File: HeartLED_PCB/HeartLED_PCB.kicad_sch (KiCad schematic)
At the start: 33 parts, among them U1 ICM7555CBAZ, U2 CD4017BM, U3 HT7750A, U4 HX SS12F44G4

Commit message: Added LCSC and 3D models
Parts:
- BT1: LCSC (none) -> C5370859
- C1: LCSC (none) -> C1705
- C2: LCSC (none) -> C7190
- C3: footprint FOOTPRINTS:TAJA476K006RNJ -> FOOTPRINTS:TAJA226M010RNJ; LCSC (none) -> C7183
- L1: LCSC (none) -> C1034
- R1: LCSC (none) -> C15458
- R10, R11, R12, R3, R4, R5, R6, R7, R8, R9: LCSC (none) -> C25936
- R2: LCSC (none) -> C25531
- S1: LCSC (none) -> C727113
- U1: LCSC (none) -> C3304410
- U2: LCSC (none) -> C1523359
- U3: LCSC (none) -> C259884; LCSC Part C259884 -> (none)
- U4: LCSC (none) -> C5149844; LCSC Part C5149844 -> (none)
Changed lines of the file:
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@@
 			)
 		)
+		(property "LCSC" "C25936"
+			(at 96.52 78.74 90)
+			(effects
+				(font
+					(size 1.27 1.27)
+				)
+				(hide yes)
+			)
+		)
 		(pin "2"
 		)
@@
 			)
 		)
+		(property "LCSC" "C25936"
+			(at 96.52 86.36 90)
+			(effects
+				(font
+					(size 1.27 1.27)
+				)
+				(hide yes)
+			)
+		)
 		(pin "2"
 		)
@@
 			)
 		)
+		(property "LCSC" "C25936"
+			(at 96.52 91.44 90)
+			(effects
+				(font
+					(size 1.27 1.27)
+				)
+				(hide yes)
+			)
+		)
 		(pin "2"
 		)
@@
 			)
 		)
+		(property "LCSC" "C25936"
+			(at 96.52 88.9 90)
+			(effects
+				(font
+					(size 1.27 1.27)
+				)
+				(hide yes)
+			)
+		)
 		(pin "2"
 		)
@@
 			)
 		)
+		(property "LCSC" "C25936"
+			(at 96.52 71.12 90)
+			(effects
+				(font
+					(size 1.27 1.27)
+				)
+				(hide yes)
+			)
+		)
 		(pin "2"
 		)
@@
 			)
 		)
+		(property "LCSC" "C7190"
+			(at 40.64 172.72 0)
+			(effects
+				(font
+					(size 1.27 1.27)
+				)
+				(hide yes)
+			)
+		)
 		(pin "2"
 		)
@@
 			)
 		)
+		(property "LCSC" "C15458"
+			(at 20.32 26.67 90)
+			(effects
+				(font
+					(size 1.27 1.27)
+				)
+				(hide yes)
+			)
+		)
 		(pin "2"
 		)
@@
 			)
 		)
+		(property "LCSC" "C1705"
+			(at 20.32 31.75 90)
+			(effects
+				(font
+					(size 1.27 1.27)
+				)
+				(hide yes)
+			)
+		)
 		(pin "2"
 		)
@@
 			)
 		)
+		(property "LCSC" "C3304410"
+			(at 58.42 29.21 0)
+			(effects
+				(font
+					(size 1.27 1.27)
+				)
+				(hide yes)
+			)
+		)
 		(pin "7"
 		)
@@
 			)
 		)
+		(property "LCSC" "C25936"
+			(at 96.52 73.66 90)
+			(effects
+				(font
+					(size 1.27 1.27)
+				)
+				(hide yes)
+			)
+		)
 		(pin "2"
 		)
@@
 			)
 		)
-		(property "LCSC Part" "C259884"
-			(at 62.23 185.42 0)
+		(property "LCSC" "C259884"
+			(at 62.23 170.18 0)
 			(effects
 				(font
@@
 			)
 		)
+		(property "LCSC" "C5370859"
+			(at 62.23 125.73 0)
+			(effects
+				(font
+					(size 1.27 1.27)
+				)
+				(hide yes)
+			)
+		)
 		(pin "1"
 		)
@@
 			)
 		)
+		(property "LCSC" "C1523359"
+			(at 59.69 86.36 0)
+			(effects
+				(font
+					(size 1.27 1.27)
+				)
+				(hide yes)
+			)
+		)
 		(pin "2"
 		)
@@
 			)
 		)
-		(property "Footprint" "FOOTPRINTS:TAJA476K006RNJ"
+		(property "Footprint" "FOOTPRINTS:TAJA226M010RNJ"
 			(at 79.7052 176.53 0)
 			(effects
@@
 			)
 		)
+		(property "LCSC" "C7183"
+			(at 78.74 172.72 0)
+			(effects
+				(font
+					(size 1.27 1.27)
+				)
+				(hide yes)
+			)
+		)
 		(pin "1"
 		)
@@
 			)
 		)
-		(property "LCSC Part" "C5149844"
-			(at 62.23 125.73 0)
+		(property "LCSC" "C5149844"
+			(at 62.23 138.43 0)
 			(effects
 				(font
@@
 			)
 		)
+		(property "LCSC" "C25936"
+			(at 96.52 81.28 90)
+			(effects
+				(font
+					(size 1.27 1.27)
+				)
+				(hide yes)
+			)
+		)
 		(pin "2"
 		)
@@
 			)
 		)
+		(property "LCSC" "C25936"
+			(at 96.52 76.2 90)
+			(effects
+				(font
+					(size 1.27 1.27)
+				)
+				(hide yes)
+			)
+		)
 		(pin "2"
 		)
@@
 			)
 		)
+		(property "LCSC" "C25936"
+			(at 96.52 83.82 90)
+			(effects
+				(font
+					(size 1.27 1.27)
+				)
+				(hide yes)
+			)
+		)
 		(pin "2"
 		)
@@
 			)
 		)
+		(property "LCSC" "C25531"
+			(at 90.17 26.67 90)
+			(effects
+				(font
+					(size 1.27 1.27)
+				)
+				(hide yes)
+			)
+		)
 		(pin "2"
 		)
@@
 			)
 		)
+		(property "LCSC" "C727113"
+			(at 62.23 157.48 0)
+			(effects
+				(font
+					(size 1.27 1.27)
+				)
+				(hide yes)
+			)
+		)
 		(pin "1"
 		)
@@
 			)
 		)
+		(property "LCSC" "C25936"
+			(at 96.52 68.58 90)
+			(effects
+				(font
+					(size 1.27 1.27)
+				)
+				(hide yes)
+			)
+		)
 		(pin "2"
 		)
@@
 			(effects
 				(font
+					(size 1.27 1.27)
+				)
+				(hide yes)
+			)
+		)
+		(property "LCSC" "C1034"
+			(at 45.72 157.48 90)
+			(effects
+				(font

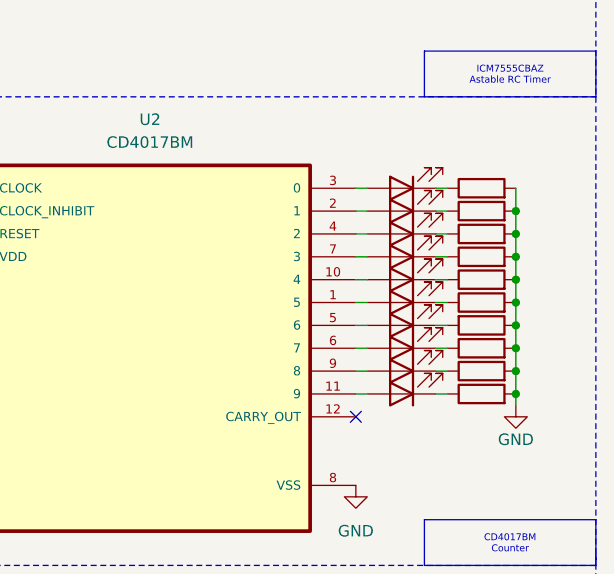
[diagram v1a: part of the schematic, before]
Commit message: Changed inductor
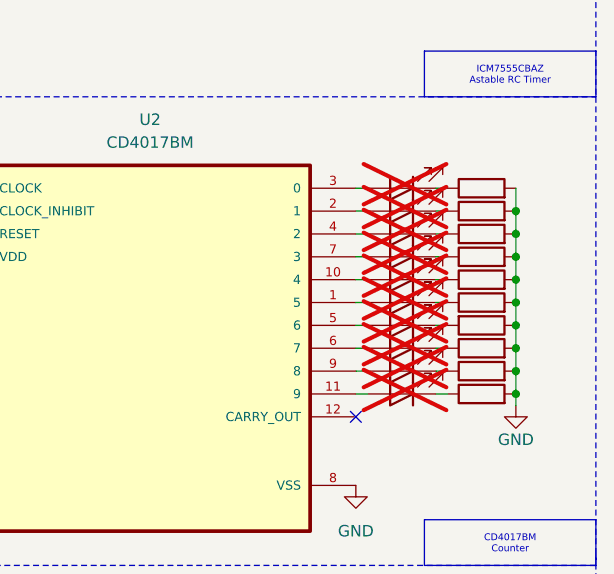
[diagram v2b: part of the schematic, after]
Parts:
- D1, D10, D2, D3, D4, D5, D6, D7, D8, D9: now not fitted
- L1: footprint FOOTPRINTS:SDFL1608Q4R7KTF -> FOOTPRINTS:SMNR5040-470MT
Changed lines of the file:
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@@
 		(in_bom yes)
 		(on_board yes)
-		(dnp no)
+		(dnp yes)
 		(fields_autoplaced yes)
 		(property "Reference" "D1"
@@
 		(in_bom yes)
 		(on_board yes)
-		(dnp no)
+		(dnp yes)
 		(fields_autoplaced yes)
 		(property "Reference" "D10"
@@
 		(in_bom yes)
 		(on_board yes)
-		(dnp no)
+		(dnp yes)
 		(fields_autoplaced yes)
 		(property "Reference" "D3"
@@
 		(in_bom yes)
 		(on_board yes)
-		(dnp no)
+		(dnp yes)
 		(fields_autoplaced yes)
 		(property "Reference" "D8"
@@
 		(in_bom yes)
 		(on_board yes)
-		(dnp no)
+		(dnp yes)
 		(fields_autoplaced yes)
 		(property "Reference" "D9"
@@
 		(in_bom yes)
 		(on_board yes)
-		(dnp no)
+		(dnp yes)
 		(fields_autoplaced yes)
 		(property "Reference" "D6"
@@
 		(in_bom yes)
 		(on_board yes)
-		(dnp no)
+		(dnp yes)
 		(fields_autoplaced yes)
 		(property "Reference" "D7"
@@
 		(in_bom yes)
 		(on_board yes)
-		(dnp no)
+		(dnp yes)
 		(fields_autoplaced yes)
 		(property "Reference" "D4"
@@
 		(in_bom yes)
 		(on_board yes)
-		(dnp no)
+		(dnp yes)
 		(fields_autoplaced yes)
 		(property "Reference" "D5"
@@
 		(in_bom yes)
 		(on_board yes)
-		(dnp no)
+		(dnp yes)
 		(fields_autoplaced yes)
 		(property "Reference" "D2"
@@
 			)
 		)
-		(property "Footprint" "FOOTPRINTS:SDFL1608Q4R7KTF"
+		(property "Footprint" "FOOTPRINTS:SMNR5040-470MT"
 			(at 45.72 157.48 0)
 			(effects

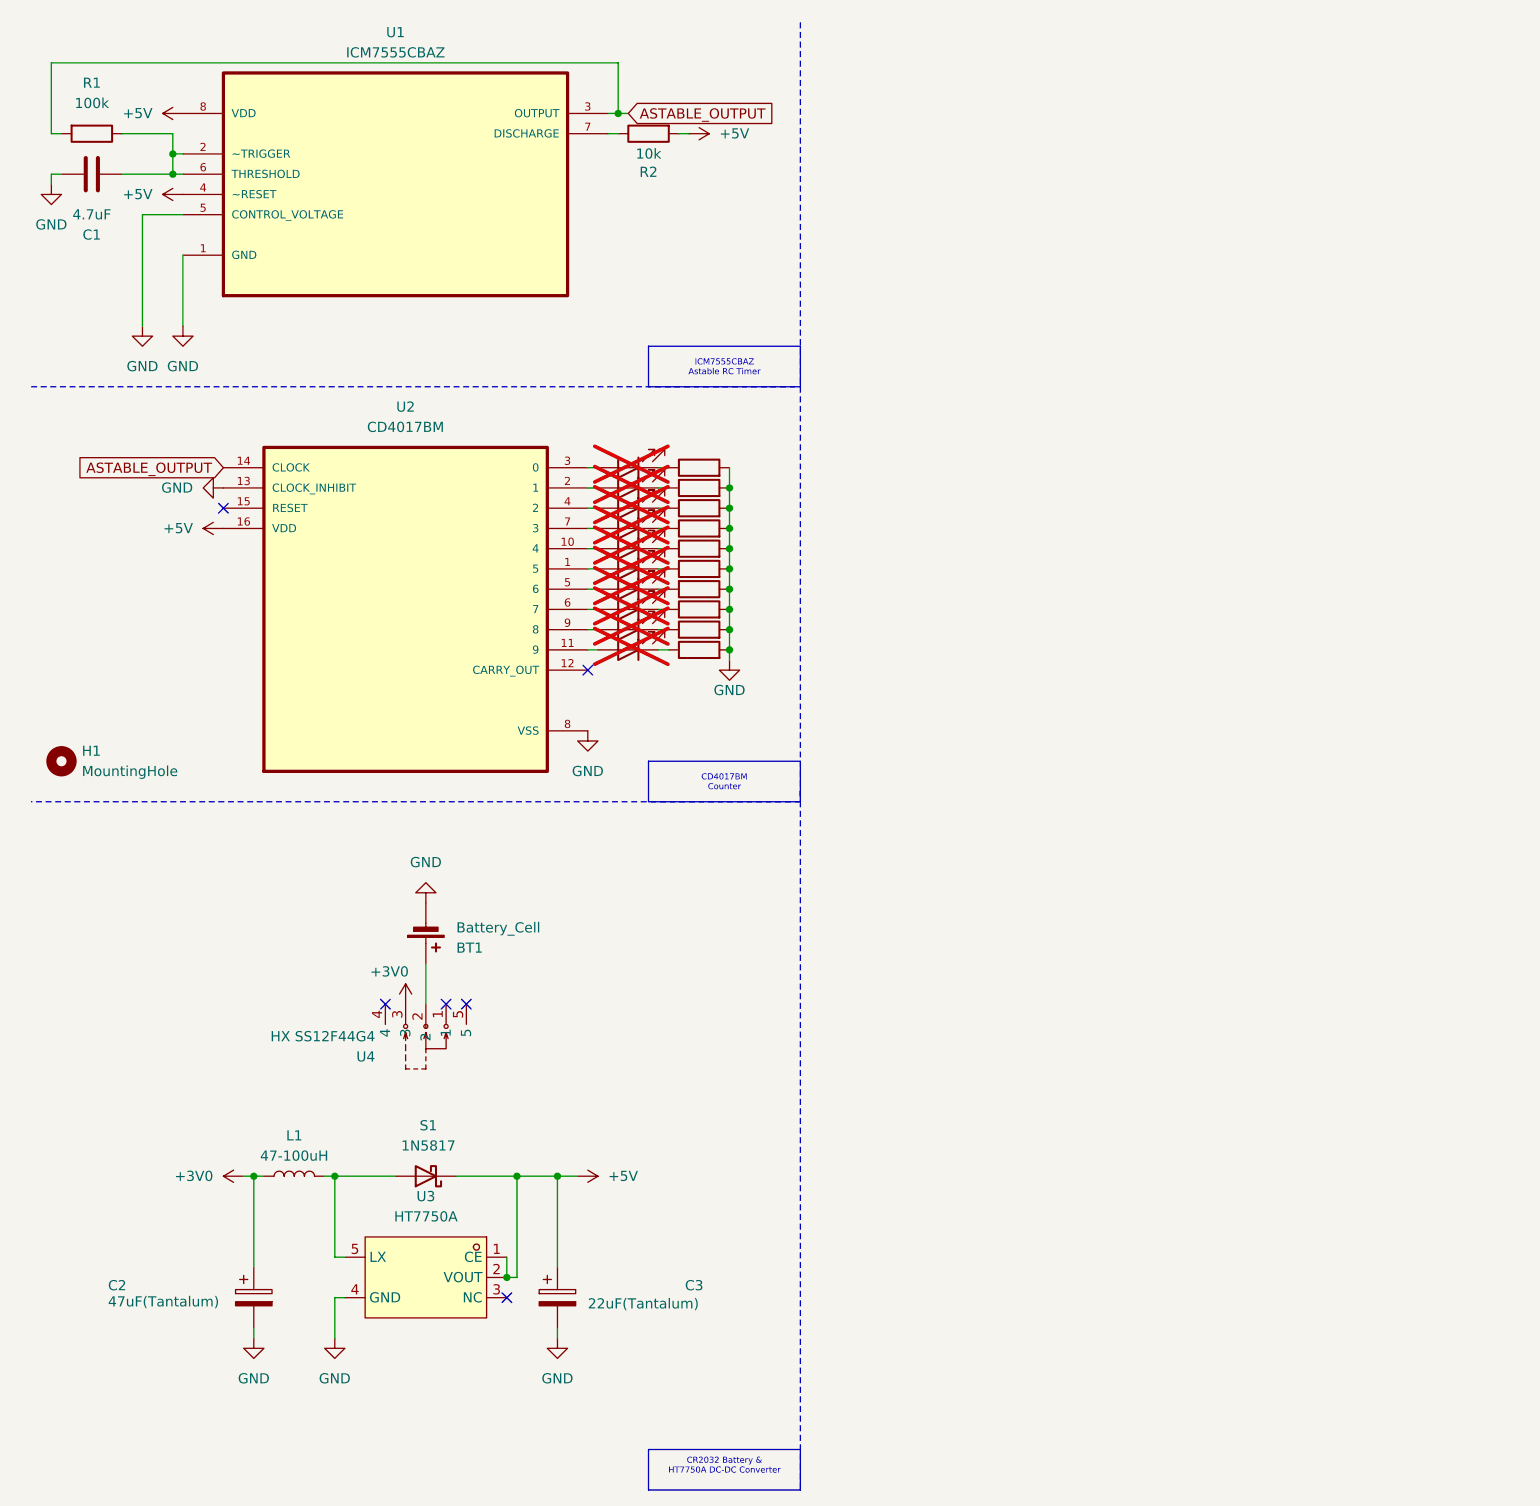
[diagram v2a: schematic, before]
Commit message: Added TestPoints and corrected track width for power nets
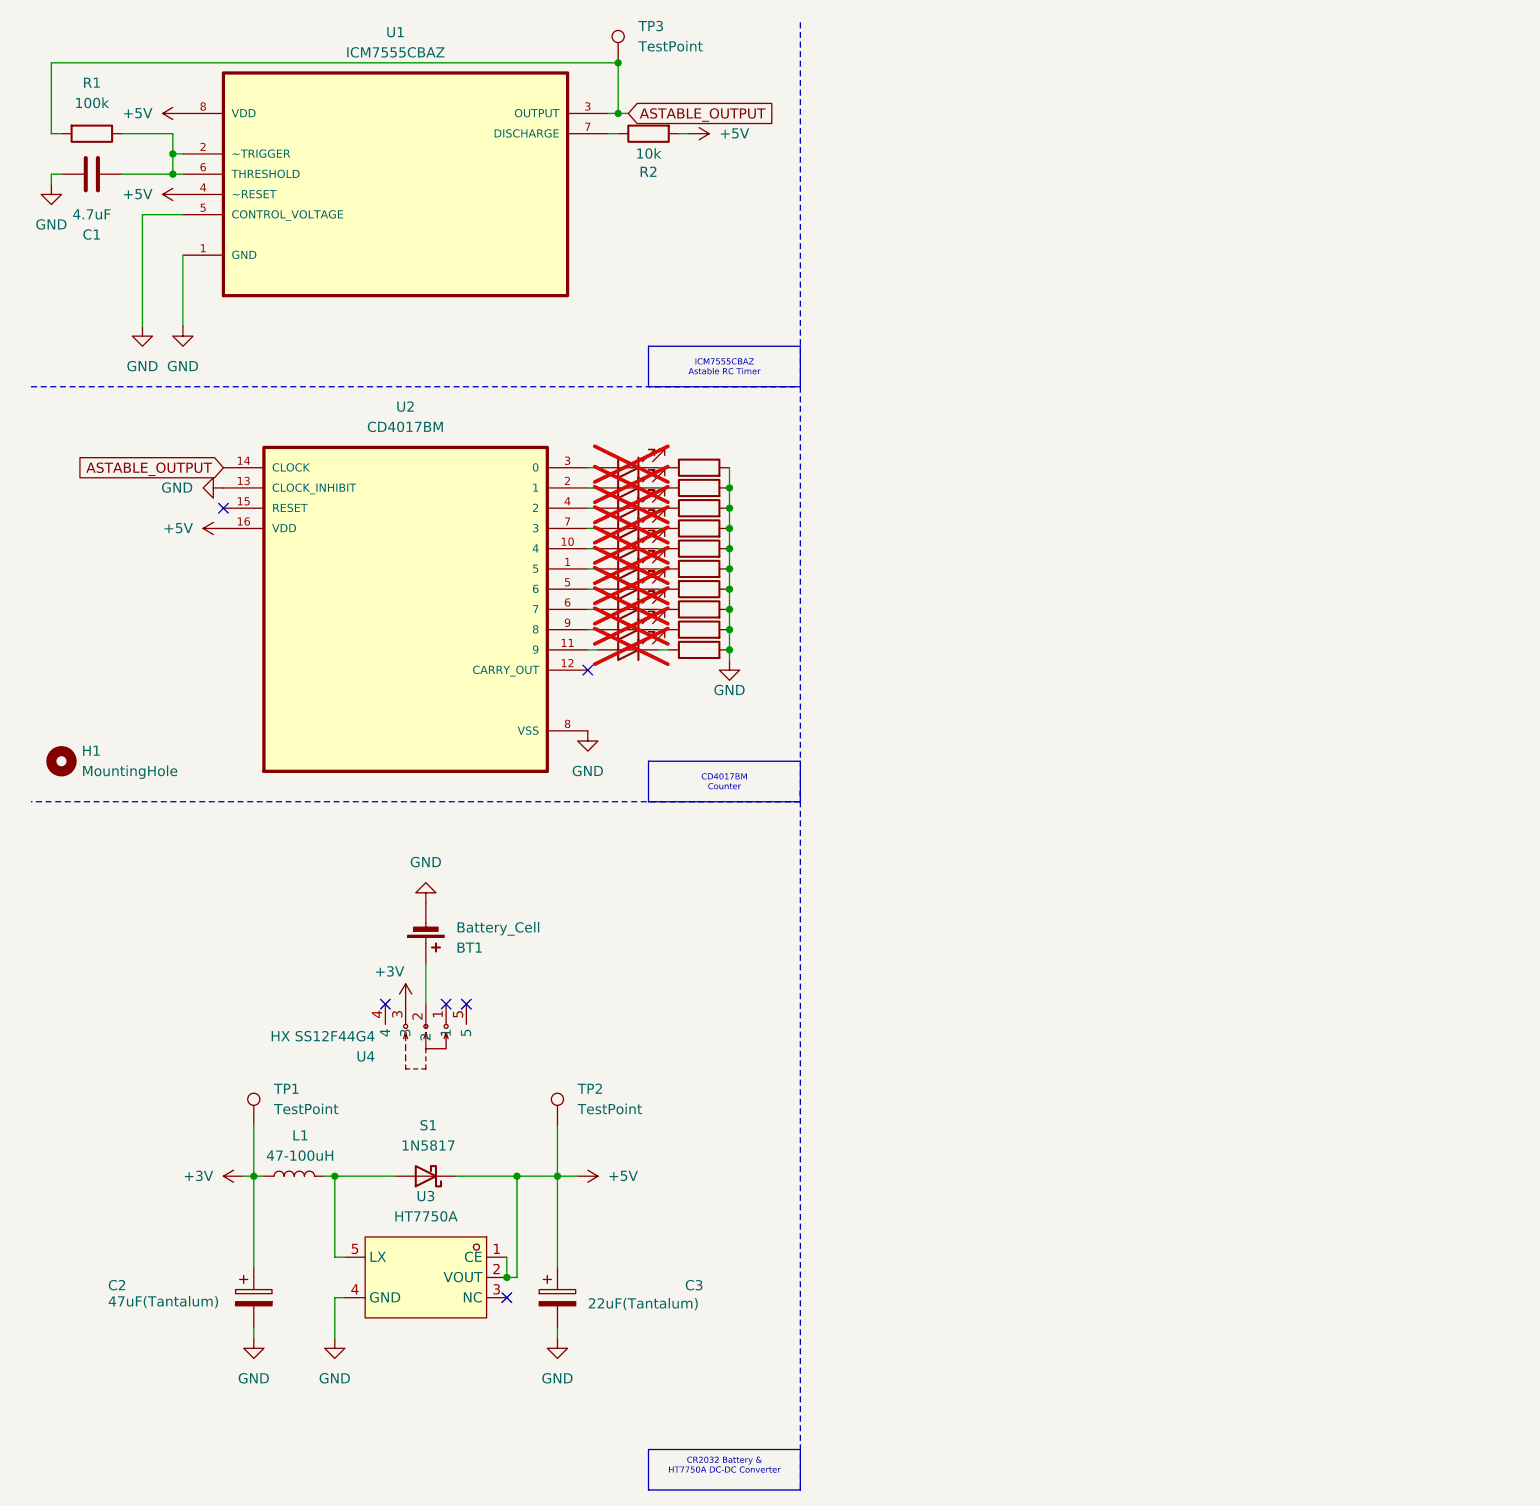
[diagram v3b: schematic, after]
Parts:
- added TP1, TP2, TP3: TestPoint, TestPoint:TestPoint_Pad_D1.0mm, symbol Connector:TestPoint
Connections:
- net +5V: now also TP2.1
- net ASTABLE_OUTPUT: now also TP3.1
- net +3V0 renamed +3V
- net +3V: now also TP1.1
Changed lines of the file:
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@@
 	)
 	(junction
+		(at 86.36 17.78)
+		(diameter 0)
+		(color 0 0 0 0)
+	)
+	(junction
 		(at 100.33 76.2)
 		(diameter 0)
@@
 	(wire
 		(pts
+			(xy 78.74 151.13) (xy 78.74 157.48)
+		)
+		(stroke
+			(width 0)
+			(type default)
+		)
+	)
+	(wire
+		(pts
 			(xy 86.36 24.13) (xy 85.09 24.13)
 		)
@@
 	(wire
 		(pts
+			(xy 40.64 151.13) (xy 40.64 157.48)
+		)
+		(stroke
+			(width 0)
+			(type default)
+		)
+	)
+	(wire
+		(pts
 			(xy 62.23 130.81) (xy 62.23 135.89)
 		)
@@
 			)
 		)
-		(property "Value" "+3V0"
+		(property "Value" "+3V"
 			(at 57.658 131.826 0)
 			(effects
@@
 			)
 		)
-		(property "Value" "+3V0"
+		(property "Value" "+3V"
 			(at 35.56 157.4799 90)
 			(effects
@@
 	)
 	(symbol
+		(lib_id "Connector:TestPoint")
+		(at 40.64 151.13 0)
+		(unit 1)
+		(exclude_from_sim no)
+		(in_bom yes)
+		(on_board yes)
+		(dnp no)
+		(fields_autoplaced yes)
+		(property "Reference" "TP1"
+			(at 43.18 146.5579 0)
+			(effects
+				(font
+					(size 1.27 1.27)
+				)
+				(justify left)
+			)
+		)
+		(property "Value" "TestPoint"
+			(at 43.18 149.0979 0)
+			(effects
+				(font
+					(size 1.27 1.27)
+				)
+				(justify left)
+			)
+		)
+		(property "Footprint" "TestPoint:TestPoint_Pad_D1.0mm"
+			(at 45.72 151.13 0)
+			(effects
+				(font
+					(size 1.27 1.27)
+				)
+				(hide yes)
+			)
+		)
+		(property "Datasheet" "~"
+			(at 45.72 151.13 0)
+			(effects
+				(font
+					(size 1.27 1.27)
+				)
+				(hide yes)
+			)
+		)
+		(property "Description" "test point"
+			(at 40.64 151.13 0)
+			(effects
+				(font
+					(size 1.27 1.27)
+				)
+				(hide yes)
+			)
+		)
+		(pin "1"
+		)
+		(instances
+			(project "HeartLED_PCB"
+				(path "/407f145c-340e-4b78-9c61-323751cc61f8"
+					(reference "TP1")
+					(unit 1)
+				)
+			)
+		)
+	)
+	(symbol
+		(lib_id "Connector:TestPoint")
+		(at 78.74 151.13 0)
+		(unit 1)
+		(exclude_from_sim no)
+		(in_bom yes)
+		(on_board yes)
+		(dnp no)
+		(fields_autoplaced yes)
+		(property "Reference" "TP2"
+			(at 81.28 146.5579 0)
+			(effects
+				(font
+					(size 1.27 1.27)
+				)
+				(justify left)
+			)
+		)
+		(property "Value" "TestPoint"
+			(at 81.28 149.0979 0)
+			(effects
+				(font
+					(size 1.27 1.27)
+				)
+				(justify left)
+			)
+		)
+		(property "Footprint" "TestPoint:TestPoint_Pad_D1.0mm"
+			(at 83.82 151.13 0)
+			(effects
+				(font
+					(size 1.27 1.27)
+				)
+				(hide yes)
+			)
+		)
+		(property "Datasheet" "~"
+			(at 83.82 151.13 0)
+			(effects
+				(font
+					(size 1.27 1.27)
+				)
+				(hide yes)
+			)
+		)
+		(property "Description" "test point"
+			(at 78.74 151.13 0)
+			(effects
+				(font
+					(size 1.27 1.27)
+				)
+				(hide yes)
+			)
+		)
+		(pin "1"
+		)
+		(instances
+			(project "HeartLED_PCB"
+				(path "/407f145c-340e-4b78-9c61-323751cc61f8"
+					(reference "TP2")
+					(unit 1)
+				)
+			)
+		)
+	)
+	(symbol
 		(lib_id "Device:C")
 		(at 20.32 31.75 270)
@@
 	)
 	(symbol
+		(lib_id "Connector:TestPoint")
+		(at 86.36 17.78 0)
+		(unit 1)
+		(exclude_from_sim no)
+		(in_bom yes)
+		(on_board yes)
+		(dnp no)
+		(fields_autoplaced yes)
+		(property "Reference" "TP3"
+			(at 88.9 13.2079 0)
+			(effects
+				(font
+					(size 1.27 1.27)
+				)
+				(justify left)
+			)
+		)
+		(property "Value" "TestPoint"
+			(at 88.9 15.7479 0)
+			(effects
+				(font
+					(size 1.27 1.27)
+				)
+				(justify left)
+			)
+		)
+		(property "Footprint" "TestPoint:TestPoint_Pad_D1.0mm"
+			(at 91.44 17.78 0)
+			(effects
+				(font
+					(size 1.27 1.27)
+				)
+				(hide yes)
+			)
+		)
+		(property "Datasheet" "~"
+			(at 91.44 17.78 0)
+			(effects
+				(font
+					(size 1.27 1.27)
+				)
+				(hide yes)
+			)
+		)
+		(property "Description" "test point"
+			(at 86.36 17.78 0)
+			(effects
+				(font
+					(size 1.27 1.27)
+				)
+				(hide yes)
+			)
+		)
+		(pin "1"
+		)
+		(instances
+			(project ""
+				(path "/407f145c-340e-4b78-9c61-323751cc61f8"
+					(reference "TP3")
+					(unit 1)
+				)
+			)
+		)
+	)
+	(symbol
 		(lib_id "power:GND")
 		(at 100.33 92.71 0)
@@
 		(on_board yes)
 		(dnp no)
-		(fields_autoplaced yes)
 		(property "Reference" "L1"
-			(at 45.72 152.4 90)
+			(at 46.482 152.4 90)
 			(effects
 				(font
@@
 		)
 		(property "Value" "47-100uH"
-			(at 45.72 154.94 90)
+			(at 46.482 154.94 90)
 			(effects
 				(font
